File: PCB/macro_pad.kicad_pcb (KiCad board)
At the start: 2 copper layers, 112.3 x 92.7 mm, 57 parts, among them J1 OLED, J2 SWD, SW1 SW_Push_45deg, SW10 SW_Push_45deg, SW11 SW_Push_45deg, SW12 SW_Push_45deg, SW13 SW_Push_45deg, SW14 SW_Push_45deg, SW15 SW_Push_45deg, SW16 SW_Push_45deg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

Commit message: Added Frame and Firmware
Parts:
- moved A1 2.67 mm to (148.1, 66.1)
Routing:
- net GND: track 61.5 -> 29.0 mm
- net /VlEncB: track 113.7 -> 117.4 mm
- net /EncB1: track 109.8 -> 113.0 mm
- net row3: track 116.9 -> 119.7 mm
- net row2: track 100.4 -> 103.2 mm
- net +3V3: track 84.3 -> 87.0 mm
- net row1: track 84.3 -> 87.0 mm
- net /SWDIO: track 38.2 -> 40.9 mm
- net /EncB2: track 56.7 -> 59.4 mm
- net /SWCLK: track 38.1 -> 40.7 mm
- net /VlEncA: track 129.0 -> 126.4 mm, vias 0 -> 1
- net /BrEncB: track 72.2 -> 74.0 mm
- net /BrEncA: track 73.4 -> 75.0 mm
- net column3: track 74.8 -> 76.0 mm
- net /LedData: track 27.8 -> 29.0 mm
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
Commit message: Followed guidelines on schem
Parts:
- removed A1: RaspberryPi_Pico, Module:RaspberryPi_Pico_SMD
- removed J1: OLED, Connector_PinSocket_2.54mm:PinSocket_1x04_P2.54mm_Vertical
- removed J2: SWD, Connector_PinHeader_2.54mm:PinHeader_1x04_P2.54mm_Vertical
- removed SW17, SW18: RotaryEncoder_Switch, RotaryEncoder_Alps_EC11E-Switch_Vertical_H20mm:RotaryEncoder_Alps_EC11E-Switch_Vertical_H20mm
- added OLED1: OLED, Connector_PinSocket_2.54mm:PinSocket_1x04_P2.54mm_Vertical, F.Cu at (100.5, 60.6)
- added XIAO1: MOUDLE-SEEEDUINO-XIAO, XIAO_RP2040:XIAO_RP2040, F.Cu at (122.1, 65.0)
- H1, H2, H3, H4: value MountingHole -> MountingHole_Pad; footprint MountingHole:MountingHole_3.2mm_M3 -> MountingHole:MountingHole_3.2mm_M3_ISO7380_Pad
- R1: moved to F.Cu
- moved H4 100.0 mm to (160.8, 157.1)
- moved H3 82.9 mm to (84.6, 157.1)
- moved H1 70.2 mm to (84.6, 58.0)
- moved G*** 45.4 mm to (143.1, 155.9), turned to 0 degrees
- moved D20 40.2 mm to (94.2, 94.8)
- moved D17 40.2 mm to (151.3, 94.8)
- moved D19 40.2 mm to (113.2, 94.8)
- moved D22 40.2 mm to (113.2, 113.9)
- moved D25 40.2 mm to (151.3, 132.9)
- moved D18 40.2 mm to (132.3, 94.8)
- moved D23 40.2 mm to (132.3, 113.9)
- moved D26 40.2 mm to (132.3, 132.9)
- moved D21 39.6 mm to (93.5, 113.9)
- moved D27 39.6 mm to (112.6, 132.9)
- moved D28 39.6 mm to (93.5, 132.9)
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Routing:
- net /VlEncA: track 126.4 -> 0.00 mm, vias 1 -> 0
- net /VlEncB: track 117.4 -> 0.00 mm, vias 1 -> 0
- net /EncB1: track 113.0 -> 0.00 mm, vias 1 -> 0
- net +3V3: track 87.0 -> 0.00 mm, vias 1 -> 0
- net /BrEncA: track 75.0 -> 0.00 mm, vias 1 -> 0
- net /BrEncB: track 74.0 -> 0.00 mm, vias 1 -> 0
- net row3: track 119.7 -> 184.4 mm
- net /EncB2: track 59.4 -> 0.00 mm, vias 1 -> 0
- net row2: track 103.2 -> 160.8 mm, vias 0 -> 1
- net /SCL: track 71.7 -> 16.8 mm
- net /SDA: track 69.9 -> 17.2 mm
- net row1: track 87.0 -> 133.6 mm, vias 0 -> 1
- net column0: track 136.3 -> 92.6 mm
- net /SWDIO: track 40.9 -> 0.00 mm
- net /SWCLK: track 40.7 -> 0.00 mm
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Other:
- board size 112.3 x 92.7 mm -> 86.4 x 109.2 mm

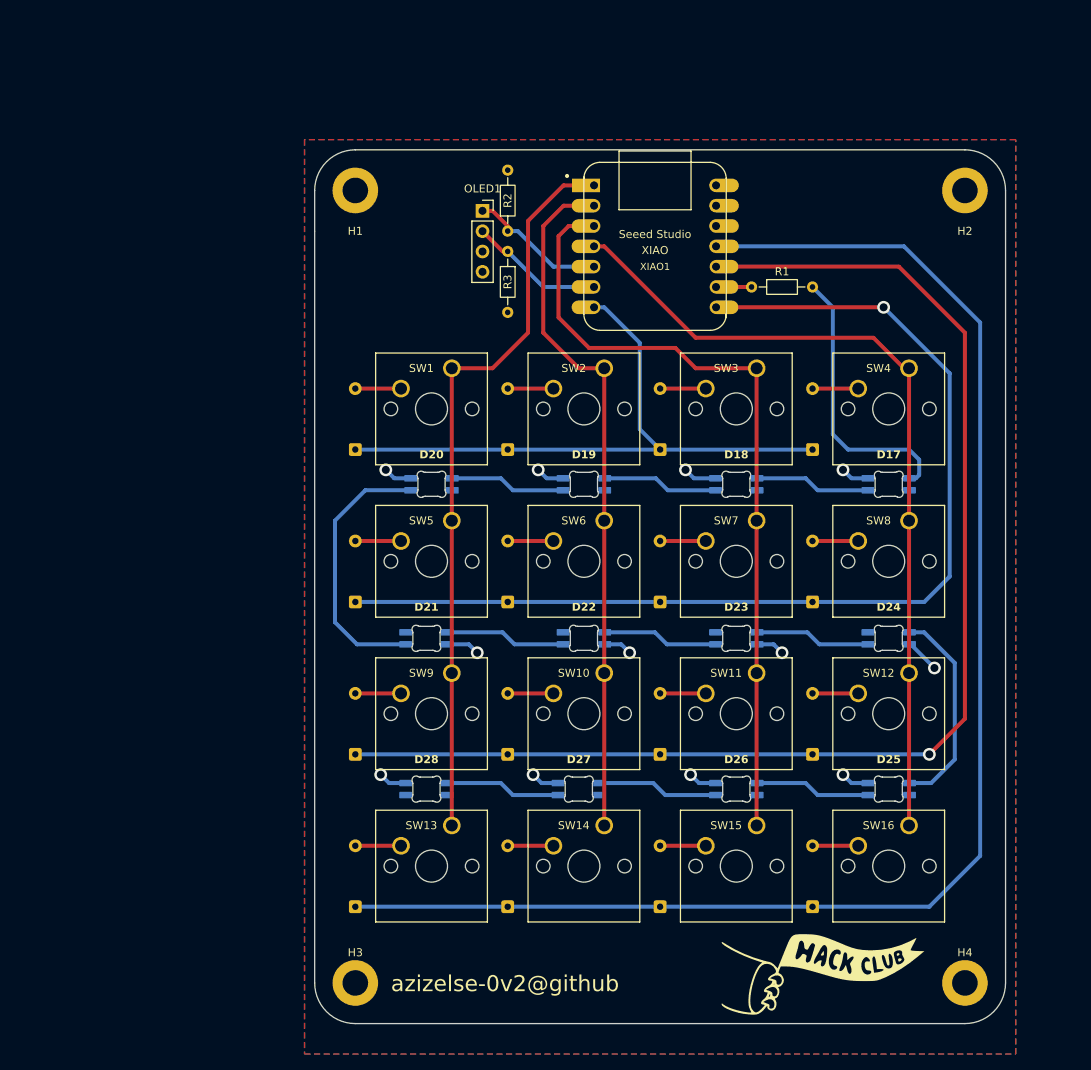
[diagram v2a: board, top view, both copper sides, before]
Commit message: Changed Microcontroller and size of pcb
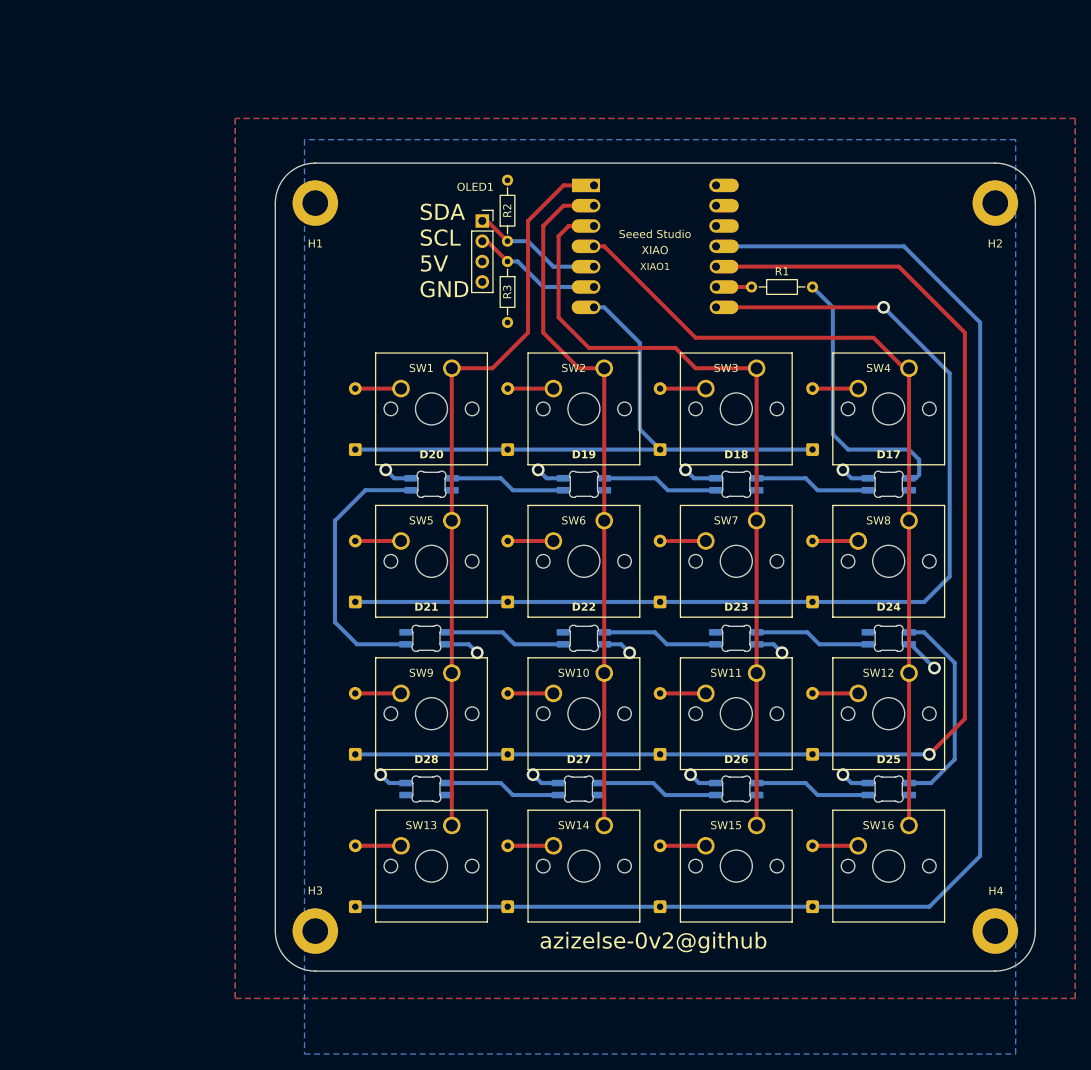
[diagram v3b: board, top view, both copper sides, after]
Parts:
- removed G***: LOGO, LOGO
- moved H3 8.18 mm to (79.6, 150.6)
- moved H4 7.51 mm to (164.6, 150.6)
- moved H1 5.24 mm to (79.6, 59.6)
- moved H2 4.12 mm to (164.6, 59.6)
- moved OLED1 1.26 mm to (100.5, 61.8)
- moved R2 1.26 mm to (103.7, 64.3)
- moved R3 1.26 mm to (103.7, 66.9)
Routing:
- net /SDA: track 17.2 -> 16.3 mm
- net /SCL: track 16.8 -> 16.3 mm
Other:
- board size 86.4 x 109.2 mm -> 95 x 101 mm
- board text added: "SDA SCL 5V GND"
- board text added: "Stop looking at my bottom."
